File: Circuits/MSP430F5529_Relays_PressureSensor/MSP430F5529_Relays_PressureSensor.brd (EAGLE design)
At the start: 107.9 x 134.6 mm, 15 parts, among them IC1 UA78M05DCY, J2 OSTTG0451XBNO_THP, K1 AQV21SMD, K2 AQV21SMD, U2 SSCMRNN015PA3A3

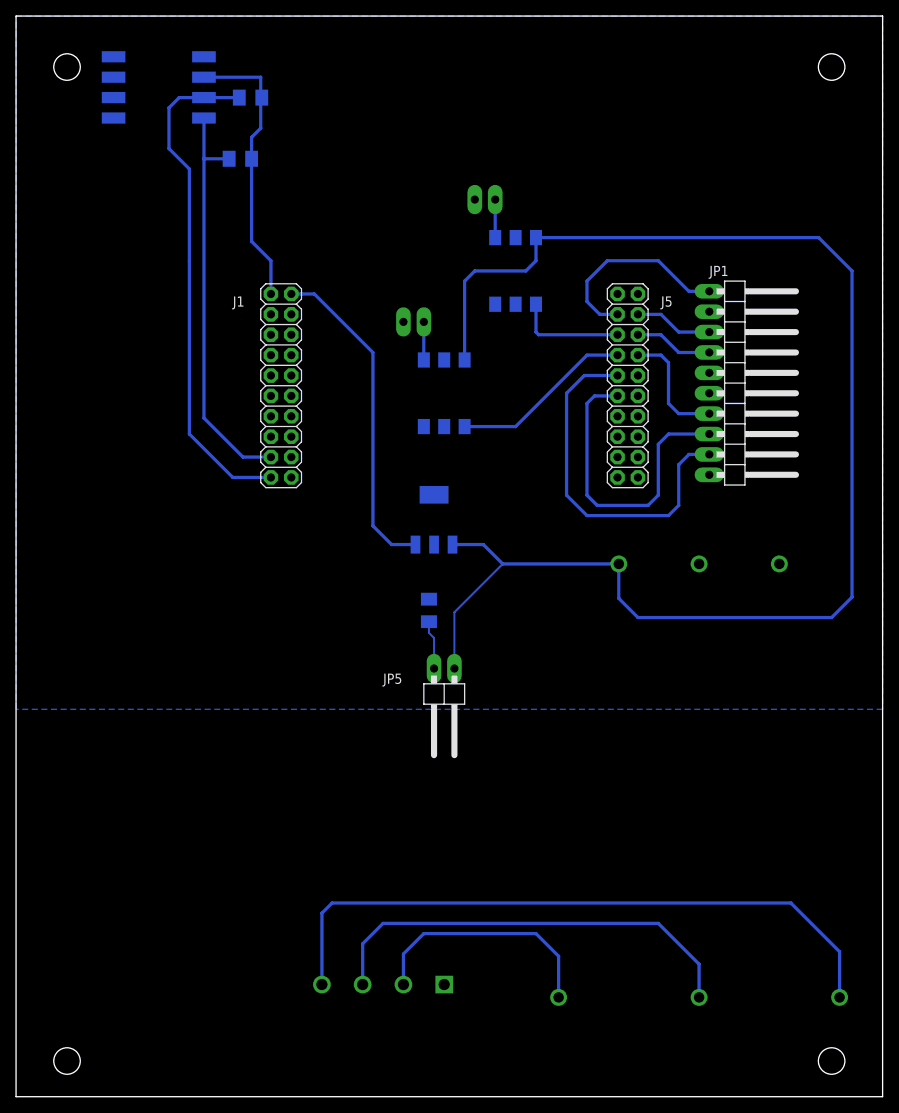
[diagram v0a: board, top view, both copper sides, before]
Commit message: Fix mistakes where power supply and terminal on bottom but use bottom traces Put both on top (top of supply will still be below LCD) and fix traces Some other minor layout adjustments (move pressure sensor closer to jumper, no reason for it to be near edge)
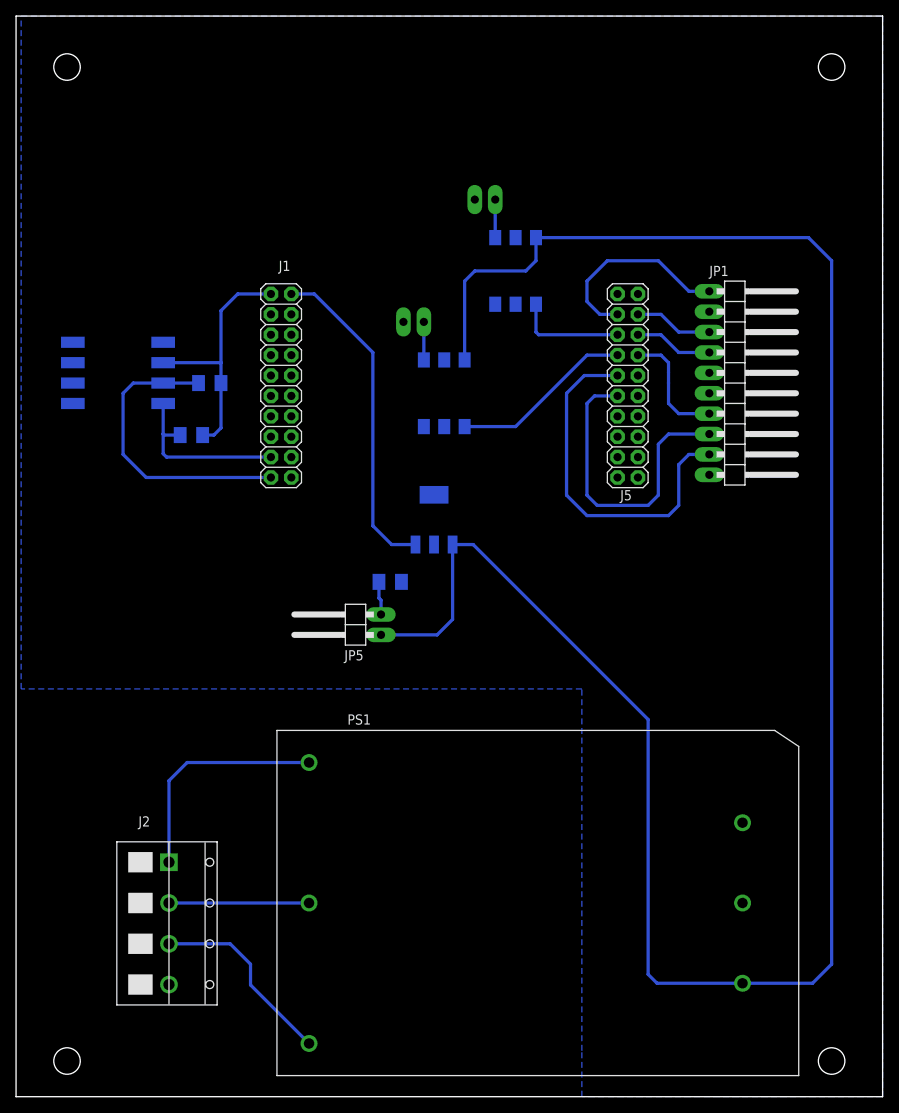
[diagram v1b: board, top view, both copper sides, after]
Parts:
- JP1: value (none) -> SWITCHES
- PS1: value YW1515ATHP -> YW1515ANO_THP; device MasterSPIS:YW15 -> MasterSPIS:YW15_NO_THP
- moved R1 35.9 mm to (-1.27, 24.1)
- moved U2 35.9 mm to (-12.7, 25.4)
- moved R2 35.0 mm to (-3.56, 17.7)
- moved J2 27.7 mm to (-6.35, -43.2), flipped to the top, turned to 270 degrees
- moved PS1 26.4 mm to (38.1, -40.6), flipped to the top, turned to 0 degrees
- moved JP5 14.9 mm to (16.3, -5.97), turned to 90 degrees
- moved R3 5.99 mm to (21.2, -0.64), turned to 0 degrees
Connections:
- net AC_L: now also J2.P3; no longer J2.P2
- net AC_N: now also J2.P2; no longer J2.P3
- net FG: now also J2.P1; no longer J2.P4
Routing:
- net 12V: track 177.0 -> 256.8 mm
- net FG: track 82.1 -> 28.5 mm
- net AC_N: track 54.3 -> 17.4 mm
- net P4.2: track 50.9 -> 22.0 mm
- net P4.1: track 63.4 -> 37.1 mm
- net AC_L: track 30.5 -> 24.1 mm
- net 3V3: track 35.7 -> 31.5 mm
- net N$1: track 6.10 -> 4.17 mm

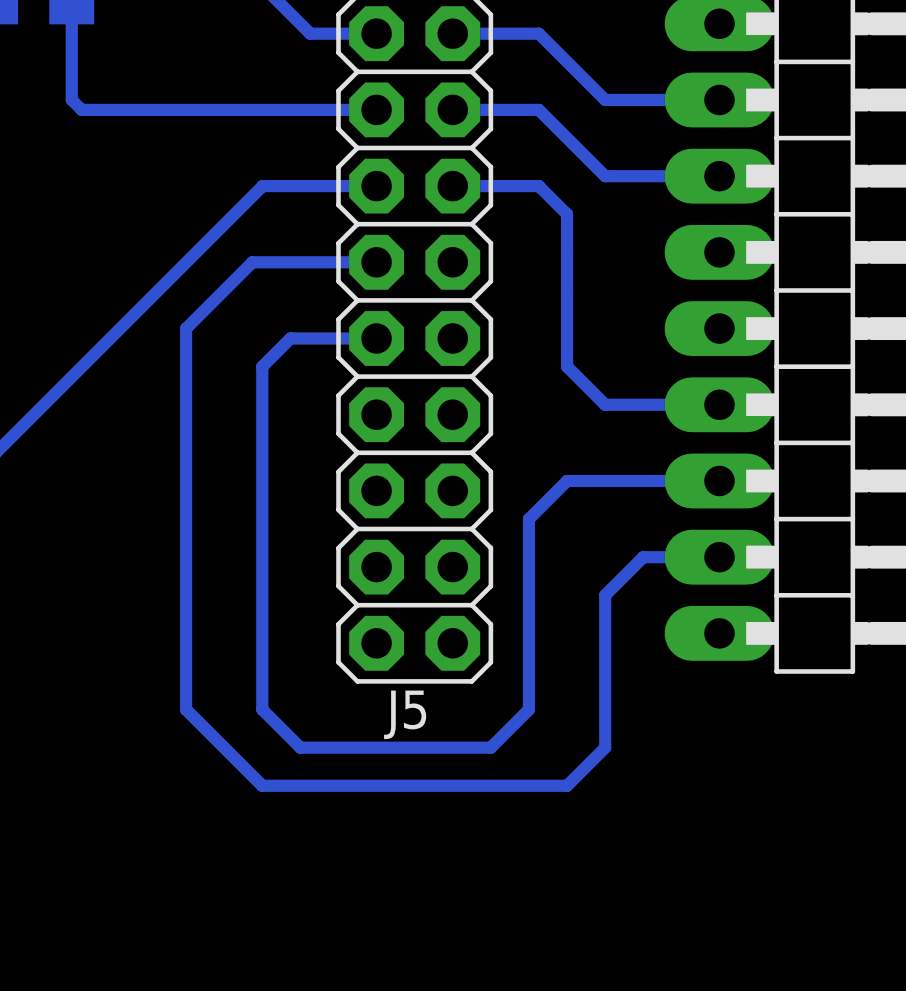
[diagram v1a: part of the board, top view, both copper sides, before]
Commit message: Replace P7.4 with P2.3 as P7.4 is not IRQ-capable
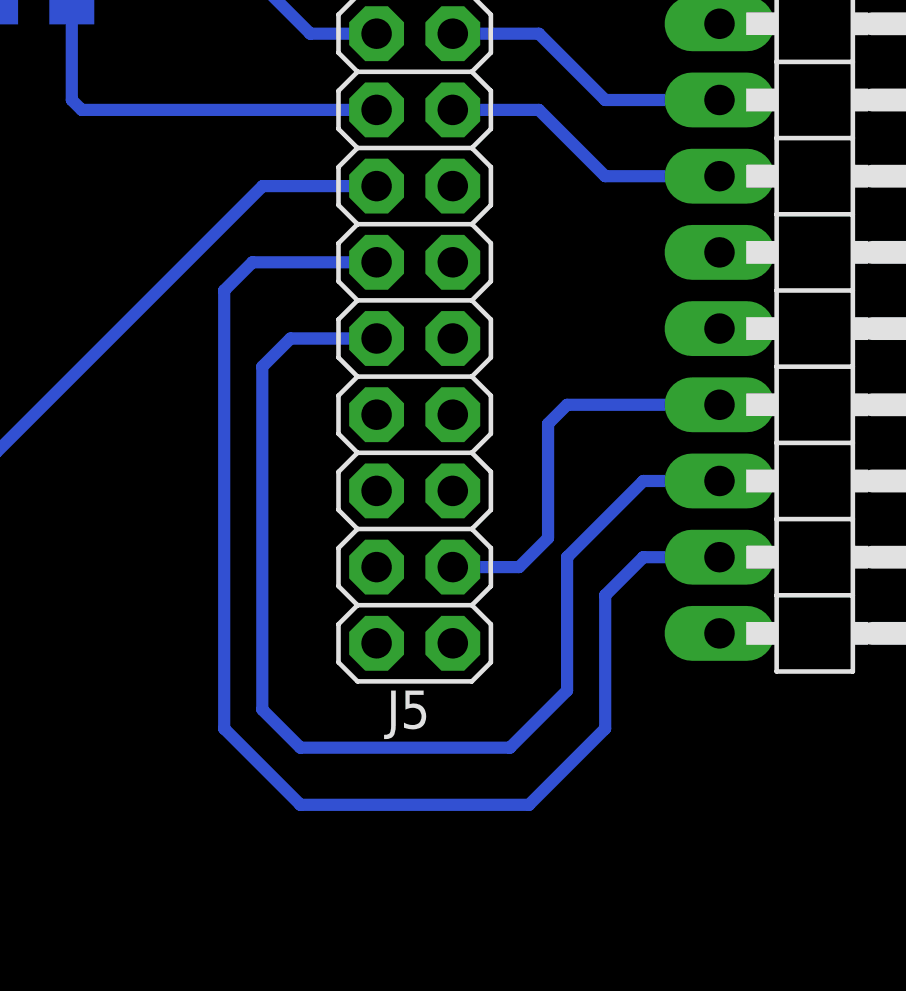
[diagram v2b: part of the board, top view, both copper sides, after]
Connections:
- new net P2.3: J5.18, JP1.7
- net P7.4: no longer JP1.7
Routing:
- net P7.4: track 14.9 -> 0.00 mm
- net P2.3: track 0.00 -> 13.4 mm
- net P1.3: track 44.9 -> 43.7 mm
- net P1.2: track 38.8 -> 37.7 mm
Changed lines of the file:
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@@
 <signal name="P7.4">
 <contactref element="J5" pad="8"/>
-<contactref element="JP1" pad="7"/>
-<wire x1="60.96" y1="20.32" x2="57.15" y2="20.32" width="0.4064" layer="16"/>
-<wire x1="57.15" y1="20.32" x2="55.88" y2="21.59" width="0.4064" layer="16"/>
-<wire x1="55.88" y1="21.59" x2="55.88" y2="24.13" width="0.4064" layer="16"/>
-<wire x1="55.88" y1="24.13" x2="55.88" y2="25.4" width="0.4064" layer="16"/>
-<wire x1="52.07" y1="27.6098" x2="54.9402" y2="27.6098" width="0.4064" layer="16"/>
-<wire x1="54.9402" y1="27.6098" x2="55.88" y2="26.67" width="0.4064" layer="16"/>
-<wire x1="55.88" y1="26.67" x2="55.88" y2="25.4" width="0.4064" layer="16"/>
 </signal>
 <signal name="P1.2">
 <contactref element="J5" pad="11"/>
 <contactref element="JP1" pad="8"/>
-<wire x1="60.96" y1="17.78" x2="55.88" y2="17.78" width="0.4064" layer="16"/>
-<wire x1="55.88" y1="17.78" x2="54.61" y2="16.51" width="0.4064" layer="16"/>
-<wire x1="45.72" y1="21.59" x2="45.72" y2="10.16" width="0.4064" layer="16"/>
+<wire x1="45.72" y1="10.16" x2="45.72" y2="21.59" width="0.4064" layer="16"/>
 <wire x1="46.6598" y1="22.5298" x2="45.72" y2="21.59" width="0.4064" layer="16"/>
 <wire x1="49.53" y1="22.5298" x2="46.6598" y2="22.5298" width="0.4064" layer="16"/>
-<wire x1="54.61" y1="10.16" x2="53.34" y2="8.89" width="0.4064" layer="16"/>
-<wire x1="53.34" y1="8.89" x2="46.99" y2="8.89" width="0.4064" layer="16"/>
+<wire x1="60.96" y1="17.78" x2="58.42" y2="17.78" width="0.4064" layer="16"/>
+<wire x1="58.42" y1="17.78" x2="55.88" y2="15.24" width="0.4064" layer="16"/>
+<wire x1="55.88" y1="10.795" x2="53.975" y2="8.89" width="0.4064" layer="16"/>
+<wire x1="53.975" y1="8.89" x2="46.99" y2="8.89" width="0.4064" layer="16"/>
 <wire x1="46.99" y1="8.89" x2="45.72" y2="10.16" width="0.4064" layer="16"/>
-<wire x1="54.61" y1="16.51" x2="54.61" y2="10.16" width="0.4064" layer="16"/>
+<wire x1="55.88" y1="15.24" x2="55.88" y2="10.795" width="0.4064" layer="16"/>
 </signal>
 <signal name="P1.3">
@@
 <wire x1="60.96" y1="15.24" x2="58.42" y2="15.24" width="0.4064" layer="16"/>
 <wire x1="58.42" y1="15.24" x2="57.15" y2="13.97" width="0.4064" layer="16"/>
-<wire x1="57.15" y1="13.97" x2="57.15" y2="8.89" width="0.4064" layer="16"/>
-<wire x1="57.15" y1="8.89" x2="55.88" y2="7.62" width="0.4064" layer="16"/>
-<wire x1="55.88" y1="7.62" x2="45.72" y2="7.62" width="0.4064" layer="16"/>
-<wire x1="45.72" y1="7.62" x2="43.18" y2="10.16" width="0.4064" layer="16"/>
-<wire x1="43.18" y1="10.16" x2="43.18" y2="22.86" width="0.4064" layer="16"/>
-<wire x1="45.3898" y1="25.0698" x2="43.18" y2="22.86" width="0.4064" layer="16"/>
+<wire x1="57.15" y1="9.525" x2="57.15" y2="13.97" width="0.4064" layer="16"/>
 <wire x1="49.53" y1="25.0698" x2="45.3898" y2="25.0698" width="0.4064" layer="16"/>
+<wire x1="45.3898" y1="25.0698" x2="44.45" y2="24.13" width="0.4064" layer="16"/>
+<wire x1="44.45" y1="24.13" x2="44.45" y2="9.525" width="0.4064" layer="16"/>
+<wire x1="44.45" y1="9.525" x2="46.99" y2="6.985" width="0.4064" layer="16"/>
+<wire x1="46.99" y1="6.985" x2="54.61" y2="6.985" width="0.4064" layer="16"/>
+<wire x1="54.61" y1="6.985" x2="57.15" y2="9.525" width="0.4064" layer="16"/>
 </signal>
 <signal name="V-">
@@
 <wire x1="-4.09" y1="-23.14" x2="-6.35" y2="-25.4" width="0.4064" layer="16"/>
 </signal>
+<signal name="P2.3">
+<contactref element="J5" pad="18"/>
+<contactref element="JP1" pad="7"/>
+<wire x1="55.88" y1="20.32" x2="60.96" y2="20.32" width="0.4064" layer="16"/>
+<wire x1="52.07" y1="14.9098" x2="54.2798" y2="14.9098" width="0.4064" layer="16"/>
+<wire x1="55.245" y1="15.875" x2="55.245" y2="19.685" width="0.4064" layer="16"/>
+<wire x1="55.245" y1="19.685" x2="55.88" y2="20.32" width="0.4064" layer="16"/>
+<wire x1="54.2798" y1="14.9098" x2="55.245" y2="15.875" width="0.4064" layer="16"/>
+</signal>
 </signals>
